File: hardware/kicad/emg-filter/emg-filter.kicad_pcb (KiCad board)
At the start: 4 copper layers, 50 x 40 mm, 84 parts, among them J1 Conn_01x02, J10 Conn_01x02, J11 Conn_01x02, J2 Conn_01x05, J3 Conn_01x02, J4 Conn_01x02, J5 Conn_01x02, J6 Conn_01x02, J7 Conn_01x02, J8 Conn_01x02, J9 Conn_01x02, U1 LM4565, U2 LM4565, U3 LM4565, U4 LM4565, U5 LM4565, U6 LM4565, U7 INA2332

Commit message: Amplifier done
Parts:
- C15, C16, C18, C23: moved to B.Cu
- moved C22 48.5 mm to (86.4, 122.0), turned to 180 degrees
- moved C19 39.1 mm to (87.1, 108.0), turned to 180 degrees
- moved C18 37.9 mm to (86.1, 117.9)
- moved R38 36.4 mm to (86.4, 119.9), turned to 0 degrees
- moved U6 33.8 mm to (87.4, 112.1), turned to 270 degrees
- moved R31 32.8 mm to (87.1, 110.1), turned to 180 degrees
- moved C23 29.6 mm to (86.7, 112.1)
- moved C16 4.79 mm to (92.5, 112.1), turned to 0 degrees
- moved C15 3.35 mm to (91.9, 117.9), turned to 0 degrees
- moved C21 1.08 mm to (77.5, 120.3)
- moved R35 1.08 mm to (81.0, 120.3)
- moved U5 1.06 mm to (93.2, 112.1)
- moved R27 1.06 mm to (92.8, 110.1)
- moved R28 1.06 mm to (92.8, 108.1)
- moved R29 1.06 mm to (92.2, 121.9)
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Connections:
- J2 pad 1: -5V -> +5V
- J2 pad 5: +5V -> -5V
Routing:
- net Net-(C22-Pad2): track 0.00 -> 13.2 mm, vias 0 -> 1
- net Net-(C19-Pad2): track 0.00 -> 13.1 mm, vias 0 -> 1
- net /emg_module/sheet625420F9/BP_NOTCH: track 0.00 -> 4.33 mm
- net /emg_module/sheet625420FA/BP_NOTCH: track 0.00 -> 4.28 mm
- net Net-(C21-Pad2): track 3.59 -> 5.84 mm
- net Net-(C21-Pad1): track 0.00 -> 1.64 mm
- net +5V: track 16.5 -> 17.6 mm, vias 4 -> 5
- net /emg_module/OUT_A: track 10.5 -> 9.78 mm
- net /emg_module/OUT_B: track 9.73 -> 8.98 mm
- net Net-(C20-Pad2): track 5.43 -> 6.18 mm
- net -5V: track 7.78 -> 8.19 mm, vias 2 -> 3

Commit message: update
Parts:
- moved R5 51.6 mm to (15.2, 69.9), turned to 270 degrees
- moved R2 50.5 mm to (17.5, 61.0)
- moved C5 46.1 mm to (20.8, 68.5)
- moved R4 45.6 mm to (29.2, 62.2)
- moved C3 33.6 mm to (28.2, 67.2)
- moved C4 25.1 mm to (28.5, 73.0)
- moved U1 11.4 mm to (41.2, 61.5)
- moved U2 6.60 mm to (53.8, 53.0)

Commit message: Done - Ready for manufacturing
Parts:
- C1, C2, C9: moved to B.Cu
- C10, C3: value 20n -> 0.1u; moved to B.Cu
- C11, C12, C4: value 10n -> 0.1u; moved to B.Cu
- C13, C6, C7: value 0.1u -> 20n
- C14: value 0.1u -> 10n
- C15: value 0.1u -> 10n; moved to F.Cu
- C19: value 2n -> 0.1u; moved to B.Cu
- C21: value 20n -> 10n
- C22: value 2n -> 10n
- C5: value 10n -> 2n
- C8: value 0.1u -> 2n
- R11: value 133k -> 191k
- R12: value 10k -> 261k
- R13, R26: value 5k -> 10k
- R14, R27: value 10k -> 132k
- R15, R17: value 132k -> 133k
- R16: value 133k -> 132k
- R18, R22: value 133k -> 10k
- R19: value 10k -> 2k
- R2: value 132k -> 2k
- R20, R28: value 2k -> 133k
- R23, R30, R33, R36: value 10k -> 133k
- R24: value 133k -> 10k; moved to B.Cu
- R25: value 10k -> 5k
- R29: value 2k -> 132k
- R3: value 133k -> 2k
- R31, R35: value 261k -> 10k
- R32: value 191k -> 2k
- R34: value 261k -> 133k
- R37: value 191k -> 10k; moved to B.Cu
- R38: value 261k -> 5k
- R4: value 132k -> 10k
- R5, R8, R9: value 133k -> 261k
- R6: value 10k -> 191k
- R7: value 2k -> 10k
- U3: value LM4565 -> INA2332; footprint emg-filter:LM4565 -> Package_SO:TSSOP-14_4.4x5mm_P0.65mm
- U7: value INA2332 -> LM4565; footprint Package_SO:TSSOP-14_4.4x5mm_P0.65mm -> emg-filter:LM4565
- moved R2 88.4 mm to (92.3, 108.1)
- moved R4 84.9 mm to (91.7, 119.8), turned to 180 degrees
- moved R5 80.9 mm to (85.5, 110.1), turned to 180 degrees
- moved C5 75.9 mm to (85.5, 108.0), turned to 180 degrees
- moved R16 72.6 mm to (69.8, 128.3), turned to 270 degrees
- moved U1 72.1 mm to (92.7, 112.1), turned to 270 degrees
- moved R21 71.8 mm to (82.9, 131.0), turned to 270 degrees
- moved C4 71.8 mm to (84.5, 117.9), turned to 180 degrees
- moved C12 71.2 mm to (90.9, 130.8), turned to 180 degrees
- moved R25 70.7 mm to (95.6, 130.4), turned to 180 degrees
- moved R18 69.4 mm to (87.7, 126.9)
- moved U4 69.3 mm to (84.8, 128.7), turned to 180 degrees
- moved R14 68.9 mm to (70.6, 131.1)
- moved U2 67.2 mm to (85.8, 112.1), turned to 270 degrees
- moved C3 67.0 mm to (75.2, 115.0)
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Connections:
- C1 pad 1: +5V -> GND
- C1 pad 2: GND -> +5V
- C10 pad 1: Net-(C10-Pad1) -> GND
- C10 pad 2: Net-(C10-Pad2) -> -5V
- C11 pad 1: Net-(C11-Pad1) -> +5V
- C11 pad 2: /emg_module/sheet625420FA/BP_NOTCH -> GND
- C12 pad 1: Net-(C12-Pad1) -> +5V
- C12 pad 2: Net-(C11-Pad1) -> GND
- C13 pad 1: GND -> Net-(C13-Pad1)
- C13 pad 2: -5V -> Net-(C13-Pad2)
- C14 pad 1: -5V -> Net-(C14-Pad1)
- C14 pad 2: GND -> /emg_module/sheet625420F9/BP_NOTCH
- C15 pad 1: GND -> Net-(C15-Pad1)
- C15 pad 2: +5V -> Net-(C14-Pad1)
- C16 pad 1: -5V -> GND
- C16 pad 2: GND -> -5V
- C17 pad 1: GND -> -5V
- C17 pad 2: +5V -> GND
- C19 pad 1: /emg_module/sheet625420FA/BP_NOTCH -> +5V
- C19 pad 2: Net-(C19-Pad2) -> GND
- C2 pad 1: +5V -> -5V
- C21 pad 2: Net-(C21-Pad2) -> /emg_module/sheet625420FA/BP_NOTCH
- C22 pad 1: /emg_module/sheet625420F9/BP_NOTCH -> Net-(C22-Pad1)
- C22 pad 2: Net-(C22-Pad2) -> Net-(C21-Pad1)
- C24 pad 1: GND -> -5V
- C24 pad 2: -5V -> GND
- C3 pad 1: Net-(C3-Pad1) -> GND
- C3 pad 2: Net-(C3-Pad2) -> +5V
- C4 pad 1: Net-(C4-Pad1) -> +5V
- C4 pad 2: /emg_module/sheet625420F9/BP_NOTCH -> GND
- C5 pad 1: Net-(C5-Pad1) -> /emg_module/sheet625420FA/BP_NOTCH
- C5 pad 2: Net-(C4-Pad1) -> Net-(C5-Pad2)
- C6 pad 1: GND -> Net-(C6-Pad1)
- C6 pad 2: -5V -> Net-(C6-Pad2)
- C7 pad 1: -5V -> Net-(C7-Pad1)
- C7 pad 2: GND -> Net-(C7-Pad2)
- C8 pad 1: +5V -> /emg_module/sheet625420F9/BP_NOTCH
- C8 pad 2: GND -> Net-(C8-Pad2)
- C9 pad 1: +5V -> GND
- C9 pad 2: GND -> -5V
- R1 pad 1: Net-(D2-Pad2) -> /emg_module/OUT_A
- R1 pad 2: Net-(D1-Pad1) -> Net-(R1-Pad2)
- R10 pad 1: Net-(R10-Pad1) -> /emg_module/REF_B
- R11 pad 1: GND -> Net-(C7-Pad2)
- R11 pad 2: Net-(R11-Pad2) -> Net-(R10-Pad2)
- R12 pad 1: /emg_module/sheet625420F9/RECT_AMP -> Net-(C8-Pad2)
- R12 pad 2: Net-(R10-Pad1) -> /emg_module/sheet625420F9/BP_NOTCH
- R13 pad 2: Net-(R10-Pad1) -> Net-(D1-Pad1)
- R14 pad 1: Net-(D4-Pad2) -> Net-(R14-Pad1)
- R14 pad 2: Net-(D3-Pad1) -> Net-(C13-Pad2)
- R15 pad 1: Net-(R15-Pad1) -> Net-(C13-Pad2)
- R15 pad 2: Net-(C10-Pad2) -> Net-(R15-Pad2)
- R16 pad 1: Net-(C10-Pad2) -> /emg_module/sheet625420F9/BP_NOTCH
- R16 pad 2: Net-(R16-Pad2) -> Net-(R14-Pad1)
- R17 pad 1: /emg_module/sheet625420FA/BP_NOTCH -> Net-(R15-Pad2)
- R17 pad 2: Net-(R15-Pad1) -> Net-(C15-Pad1)
- R18 pad 1: Net-(R16-Pad2) -> Net-(R18-Pad1)
- R18 pad 2: Net-(C12-Pad1) -> Net-(D1-Pad1)
- R19 pad 2: Net-(D3-Pad1) -> Net-(R18-Pad1)
- R2 pad 1: Net-(R2-Pad1) -> Net-(R1-Pad2)
- R2 pad 2: Net-(C3-Pad2) -> GND
- R20 pad 1: Net-(R20-Pad1) -> Net-(C13-Pad1)
- R20 pad 2: Net-(R19-Pad1) -> Net-(C14-Pad1)
- R21 pad 1: Net-(C10-Pad1) -> Net-(R19-Pad1)
- R21 pad 2: Net-(C11-Pad1) -> Net-(R21-Pad2)
- R22 pad 1: Net-(R20-Pad1) -> Net-(R22-Pad1)
- R22 pad 2: Net-(R22-Pad2) -> Net-(R18-Pad1)
- R23 pad 1: Net-(R23-Pad1) -> GND
- R23 pad 2: Net-(R19-Pad1) -> Net-(R21-Pad2)
- R24 pad 1: GND -> /emg_module/sheet625420F9/RECT_AMP
- R24 pad 2: Net-(R22-Pad2) -> Net-(R22-Pad1)
- R25 pad 1: /emg_module/sheet625420FA/RECT_AMP -> Net-(D2-Pad2)
- R25 pad 2: Net-(R23-Pad1) -> Net-(R22-Pad1)
- R26 pad 2: Net-(R23-Pad1) -> Net-(D3-Pad1)
- R27 pad 1: /emg_module/OUT_A -> Net-(R27-Pad1)
- R27 pad 2: Net-(R27-Pad2) -> Net-(C20-Pad2)
- R28 pad 1: Net-(R27-Pad2) -> Net-(C20-Pad2)
- R28 pad 2: GND -> Net-(R28-Pad2)
- R29 pad 1: Net-(R29-Pad1) -> /emg_module/sheet625420FA/BP_NOTCH
- R29 pad 2: GND -> Net-(R27-Pad1)
- R3 pad 1: Net-(C3-Pad2) -> Net-(R3-Pad1)
- R3 pad 2: Net-(R3-Pad2) -> GND
- R30 pad 1: /emg_module/OUT_B -> Net-(R28-Pad2)
- R30 pad 2: Net-(R29-Pad1) -> Net-(C22-Pad1)
- R31 pad 1: /emg_module/sheet625420FA/BP_NOTCH -> Net-(R31-Pad1)
- R31 pad 2: Net-(C19-Pad2) -> Net-(D3-Pad1)
- R32 pad 2: Net-(C20-Pad2) -> Net-(R31-Pad1)
- R33 pad 1: Net-(R32-Pad1) -> Net-(C20-Pad1)
- R33 pad 2: /emg_module/REF_A -> Net-(C21-Pad1)
- R34 pad 1: Net-(C19-Pad2) -> Net-(R32-Pad1)
- R34 pad 2: Net-(C20-Pad1) -> Net-(R34-Pad2)
- R35 pad 1: Net-(C22-Pad2) -> Net-(R35-Pad1)
- R35 pad 2: Net-(C21-Pad1) -> Net-(R31-Pad1)
- R36 pad 1: /emg_module/REF_B -> GND
- R36 pad 2: Net-(R36-Pad2) -> Net-(R34-Pad2)
- R37 pad 1: Net-(C21-Pad2) -> /emg_module/sheet625420FA/RECT_AMP
- R37 pad 2: Net-(R36-Pad2) -> Net-(R35-Pad1)
- R38 pad 1: Net-(C22-Pad2) -> Net-(D4-Pad2)
- R38 pad 2: /emg_module/sheet625420F9/BP_NOTCH -> Net-(R35-Pad1)
- R4 pad 1: /emg_module/sheet625420F9/BP_NOTCH -> /emg_module/OUT_B
- R4 pad 2: Net-(R2-Pad1) -> Net-(R3-Pad1)
- R5 pad 1: Net-(R3-Pad2) -> /emg_module/sheet625420FA/BP_NOTCH
- R5 pad 2: Net-(C5-Pad1) -> Net-(C5-Pad2)
- R6 pad 1: Net-(R10-Pad2) -> Net-(R6-Pad1)
- R6 pad 2: Net-(D1-Pad1) -> Net-(C6-Pad2)
- R7 pad 1: Net-(R7-Pad1) -> Net-(R6-Pad1)
- R7 pad 2: Net-(R10-Pad2) -> /emg_module/REF_A
- R8 pad 1: Net-(C3-Pad1) -> Net-(C5-Pad2)
- R8 pad 2: Net-(C4-Pad1) -> Net-(C6-Pad1)
- R9 pad 1: Net-(R7-Pad1) -> Net-(C8-Pad2)
- R9 pad 2: Net-(R11-Pad2) -> Net-(C7-Pad1)
- U1 pad 1: Net-(R10-Pad2) -> /emg_module/OUT_A
- U1 pad 2: Net-(R10-Pad2) -> Net-(R1-Pad2)
- U1 pad 3: Net-(C5-Pad1) -> /emg_module/sheet625420FA/RECT_AMP
- U1 pad 5: Net-(R7-Pad1) -> /emg_module/sheet625420F9/RECT_AMP
- U1 pad 6: Net-(C3-Pad1) -> Net-(R3-Pad1)
- U1 pad 7: Net-(C3-Pad1) -> /emg_module/OUT_B
- U2 pad 1: Net-(D1-Pad2) -> /emg_module/sheet625420FA/BP_NOTCH
- U2 pad 2: Net-(D1-Pad1) -> Net-(C5-Pad2)
- U2 pad 6: Net-(R10-Pad1) -> Net-(C8-Pad2)
- U2 pad 7: /emg_module/sheet625420F9/RECT_AMP -> /emg_module/sheet625420F9/BP_NOTCH
- U3 pad 1: Net-(R19-Pad1) -> Net-(R6-Pad1)
- U3 pad 2: Net-(R19-Pad1) -> /emg_module/VIN_A
- U3 pad 3: Net-(C12-Pad1) -> /emg_module/sheet625420FD/+VIN_A_INA
- U3 pad 5: Net-(R20-Pad1) -> /emg_module/sheet625420FC/+VIN_B_INA
- U3 pad 6: Net-(C10-Pad1) -> /emg_module/VIN_B
- U3 pad 7: Net-(C10-Pad1) -> Net-(R10-Pad2)
- U4 pad 1: Net-(D3-Pad2) -> Net-(R18-Pad1)
- U4 pad 2: Net-(D3-Pad1) -> Net-(R18-Pad1)
- U4 pad 3: GND -> Net-(C15-Pad1)
- U4 pad 5: GND -> Net-(R19-Pad1)
- U4 pad 6: Net-(R23-Pad1) -> Net-(C13-Pad1)
- U4 pad 7: /emg_module/sheet625420FA/RECT_AMP -> Net-(C13-Pad1)
- U5 pad 1: /emg_module/OUT_A -> Net-(D1-Pad2)
- U5 pad 2: Net-(R27-Pad2) -> Net-(D1-Pad1)
- U5 pad 3: /emg_module/sheet625420FA/RECT_AMP -> GND
- U5 pad 5: /emg_module/sheet625420F9/RECT_AMP -> GND
- U5 pad 6: Net-(R29-Pad1) -> Net-(R22-Pad1)
- U5 pad 7: /emg_module/OUT_B -> /emg_module/sheet625420F9/RECT_AMP
- U6 pad 1: /emg_module/sheet625420FA/BP_NOTCH -> Net-(R31-Pad1)
- U6 pad 2: Net-(C19-Pad2) -> Net-(R31-Pad1)
- U6 pad 3: GND -> Net-(C22-Pad1)
- U6 pad 5: GND -> Net-(R32-Pad1)
- U6 pad 6: Net-(C22-Pad2) -> Net-(C20-Pad1)
- U6 pad 7: /emg_module/sheet625420F9/BP_NOTCH -> Net-(C20-Pad1)
- U7 pad 1: Net-(R32-Pad1) -> Net-(D3-Pad2)
- U7 pad 2: /emg_module/VIN_A -> Net-(D3-Pad1)
- U7 pad 3: /emg_module/sheet625420FD/+VIN_A_INA -> GND
- U7 pad 5: /emg_module/sheet625420FC/+VIN_B_INA -> GND
- U7 pad 6: /emg_module/VIN_B -> Net-(R35-Pad1)
- U7 pad 7: Net-(R36-Pad2) -> /emg_module/sheet625420FA/RECT_AMP
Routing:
- net GND: track 0.00 -> 39.2 mm, vias 0 -> 13
- net /emg_module/sheet625420FA/BP_NOTCH: track 4.28 -> 29.5 mm, vias 0 -> 2
- net /emg_module/sheet625420F9/BP_NOTCH: track 4.33 -> 29.5 mm, vias 0 -> 2
- net /emg_module/sheet625420FA/RECT_AMP: track 0.00 -> 24.6 mm, vias 0 -> 3
- net /emg_module/sheet625420F9/RECT_AMP: track 0.00 -> 24.6 mm, vias 0 -> 3
- net Net-(C15-Pad1): track 0.00 -> 13.4 mm, vias 0 -> 2
- net Net-(C22-Pad1): track 0.00 -> 13.4 mm, vias 0 -> 2
- net Net-(C22-Pad2): track 13.2 -> 0.00 mm, vias 1 -> 0
- net Net-(C19-Pad2): track 13.1 -> 0.00 mm, vias 1 -> 0
- net Net-(C8-Pad2): track 0.00 -> 13.0 mm, vias 0 -> 1
- net Net-(C5-Pad2): track 0.00 -> 12.9 mm, vias 0 -> 1
- net Net-(R31-Pad1): track 0.00 -> 12.2 mm
- net Net-(R18-Pad1): track 0.00 -> 12.2 mm
- net +5V: track 17.6 -> 29.3 mm, vias 5 -> 9
- net Net-(R35-Pad1): track 0.00 -> 11.5 mm, vias 0 -> 1
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
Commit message: Done
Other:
- board text added: "A+"
- board text added: "A-"
- board text added: "B+"
- board text added: "B-"
- board text added: "REF"

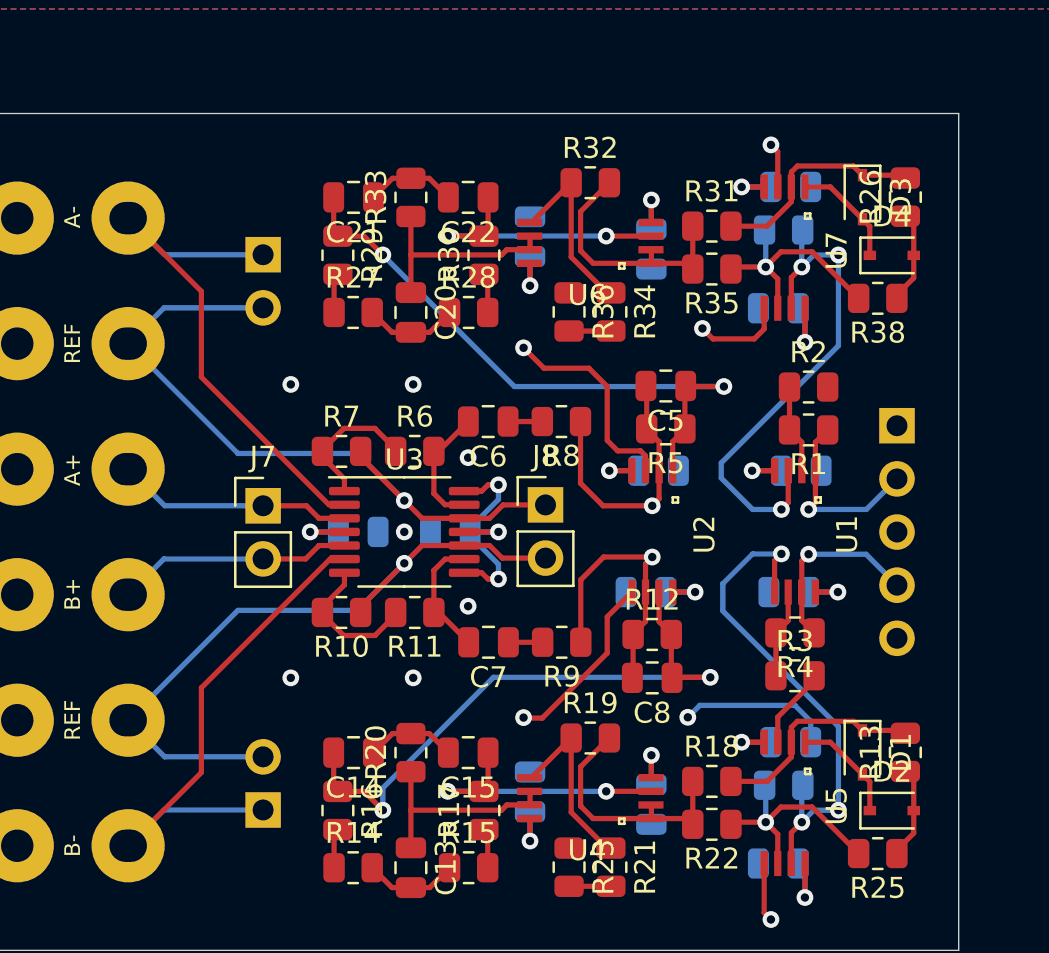
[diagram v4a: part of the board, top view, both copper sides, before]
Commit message: aligning pins to fit on motherboard
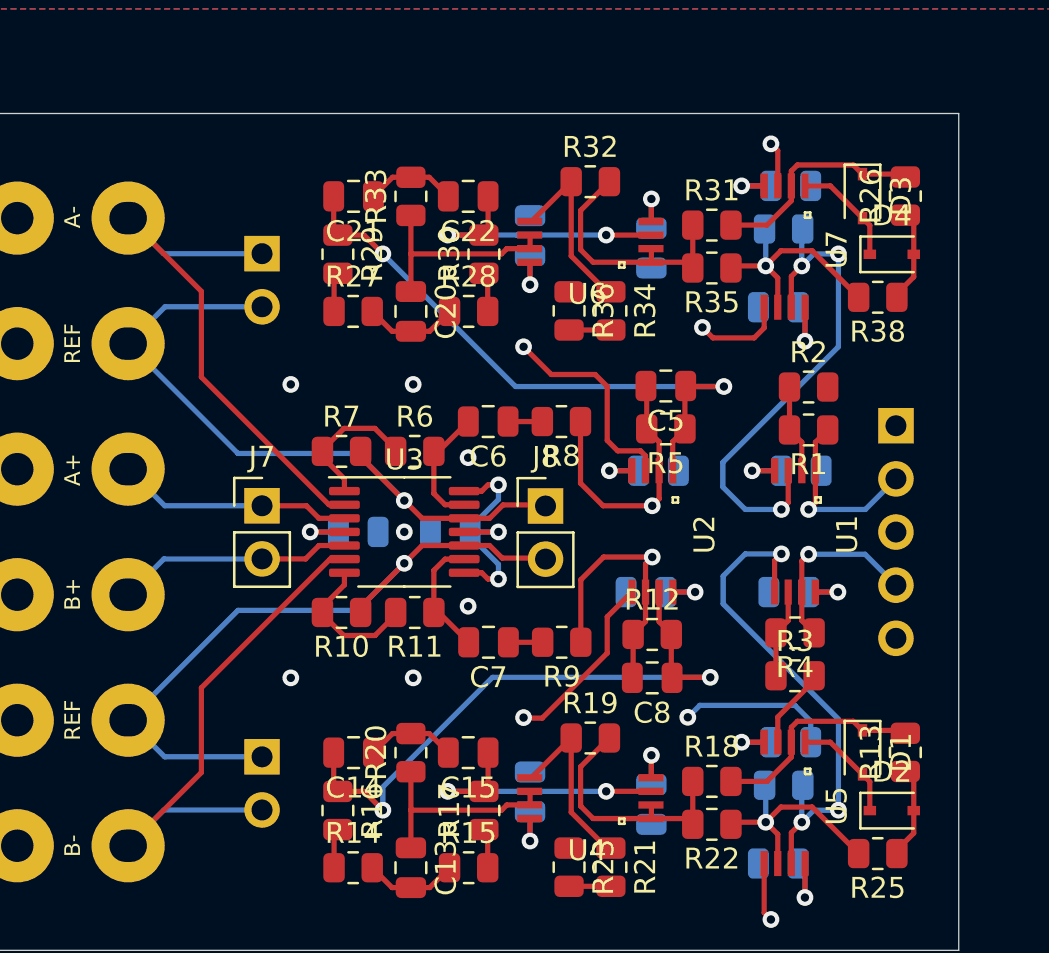
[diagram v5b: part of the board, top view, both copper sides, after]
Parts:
- moved J3 2.54 mm to (66.2, 125.8), turned to 180 degrees
- moved J1 0.07 mm to (66.2, 101.7)
- moved C18 0.05 mm to (79.0, 100.8)
- moved C20 0.05 mm to (73.3, 104.5)
- moved C21 0.05 mm to (70.6, 99.0)
- moved C22 0.05 mm to (76.1, 99.0)
- moved C24 0.05 mm to (91.5, 98.5)
- moved J8 0.05 mm to (79.8, 113.8)
- moved R27 0.05 mm to (70.6, 104.5)
- moved R28 0.05 mm to (76.1, 104.5)
- moved R29 0.05 mm to (69.8, 101.7)
- moved R30 0.05 mm to (76.8, 101.7)
- moved R31 0.05 mm to (87.7, 100.3)
- moved R33 0.05 mm to (73.3, 99.0)
- moved U7 0.05 mm to (92.2, 98.5)
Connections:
- J3 pad 1: /emg_module/VIN_B -> /emg_module/REF_B
- J3 pad 2: /emg_module/REF_B -> /emg_module/VIN_B

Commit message: fixed shematic
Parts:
- moved J7 2.54 mm to (66.2, 116.3), turned to 180 degrees
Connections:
- net /emg_module/VIN_B renamed /emg_module/-VIN_B
- J1 pad 1: /emg_module/VIN_A -> /emg_module/+VIN_A
- J4 pad 2: /emg_module/VIN_A -> /emg_module/+VIN_A
- J6 pad 2: /emg_module/sheet625420FD/+VIN_A_INA -> /emg_module/sheet625420FC/-VIN_A_INA
- J7 pad 1: /emg_module/sheet625420FD/+VIN_A_INA -> /emg_module/sheet625420FC/+VIN_B_INA
- J7 pad 2: /emg_module/sheet625420FC/+VIN_B_INA -> /emg_module/sheet625420FC/-VIN_A_INA
- U3 pad 2: /emg_module/VIN_A -> /emg_module/sheet625420FC/-VIN_A_INA
- U3 pad 3: /emg_module/sheet625420FD/+VIN_A_INA -> /emg_module/+VIN_A
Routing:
- net /emg_module/VIN_A: track 25.6 -> 0.00 mm
- net /emg_module/+VIN_A: track 0.00 -> 21.9 mm
- net /emg_module/sheet625420FC/-VIN_A_INA: track 0.00 -> 14.8 mm, vias 0 -> 1
- net /emg_module/sheet625420FD/+VIN_A_INA: track 11.3 -> 0.00 mm
- net GND: track 39.2 -> 50.2 mm, vias 13 -> 12
- net /emg_module/REF_B: track 33.9 -> 29.8 mm
- net /emg_module/REF_A: track 33.9 -> 29.8 mm
- net /emg_module/-VIN_B: track 25.5 -> 21.8 mm
- net /emg_module/sheet625420FC/+VIN_B_INA: track 11.3 -> 14.8 mm, vias 0 -> 1

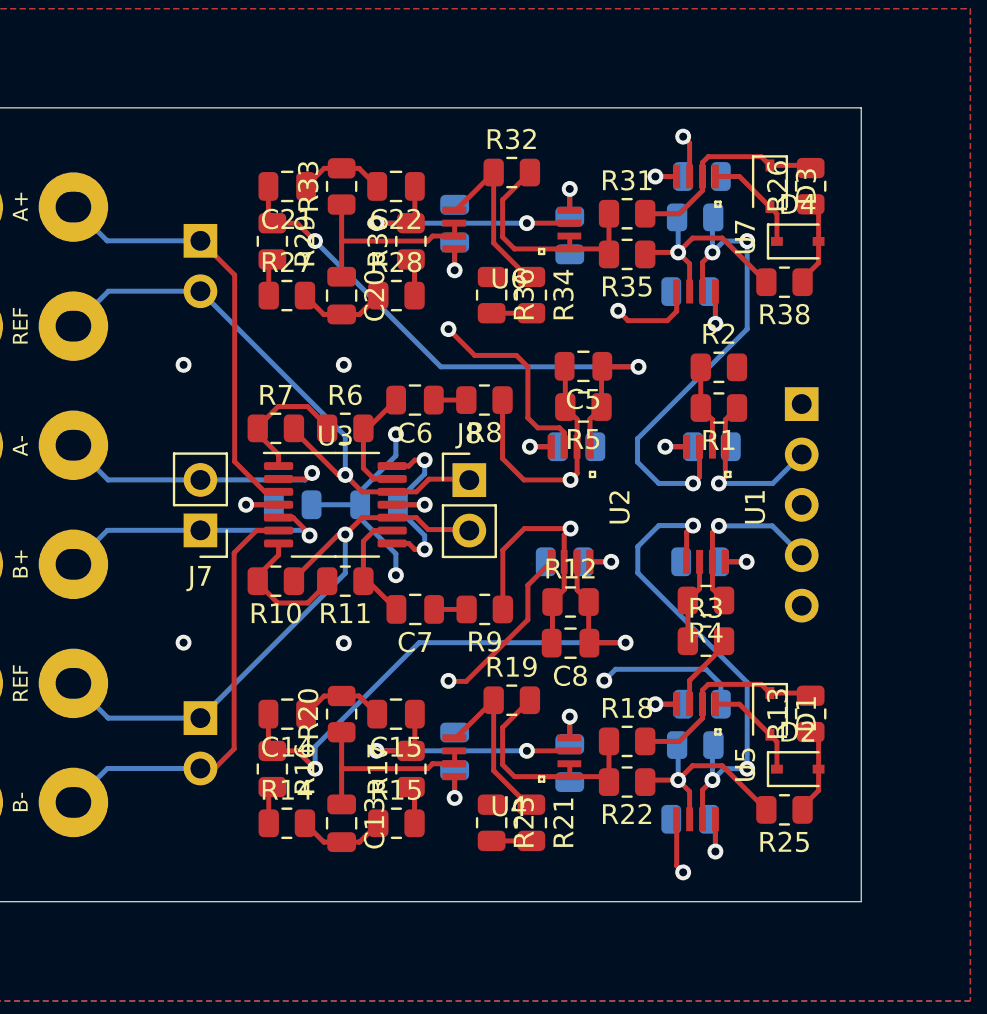
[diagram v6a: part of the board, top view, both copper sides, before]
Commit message: text layer and footprint
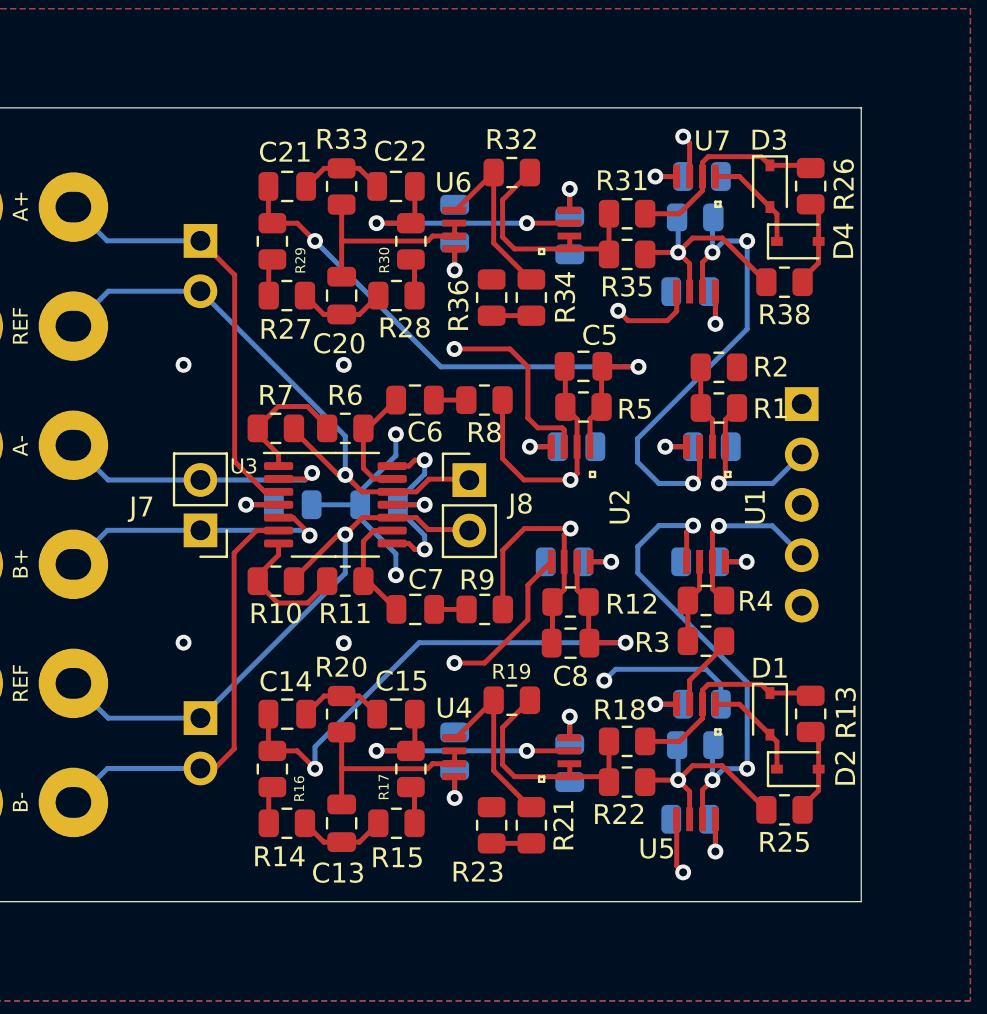
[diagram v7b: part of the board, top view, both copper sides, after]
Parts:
- moved R21 0.12 mm to (82.9, 131.2)
- moved R23 0.12 mm to (80.9, 131.2)
- moved R34 0.12 mm to (82.9, 104.6)
- moved R36 0.12 mm to (80.9, 104.6)
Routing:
- net GND: track 50.2 -> 49.2 mm

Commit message: added model number
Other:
- board text added: "+5V"
- board text added: "-5V"
- board text added: "A"
- board text added: "B"
- board text added: "GND"
- board text added: "Prosthetic Limb EMG Filter Module Concordia University Capstone 2022 220202VBKNMZSFSSHS"
